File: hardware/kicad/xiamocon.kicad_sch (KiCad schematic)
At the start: 77 parts, among them J1 JST S2B-PH-SM4-TB, J2 Conn_01x02, J3 Micro_SD_Card_Det_Hirose_DM3AT, J4 Hong Cheng HC-PM254-5.0H-2x10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, Q1 IRLML6344TRPBF, Q2 IRLML6344TRPBF, Q3 IRLML2246TRPBF, Q4 IRLML2246TRPBF, Q5 IRLML2246TRPBF, SW1 GT-TC018A-H0375-L1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

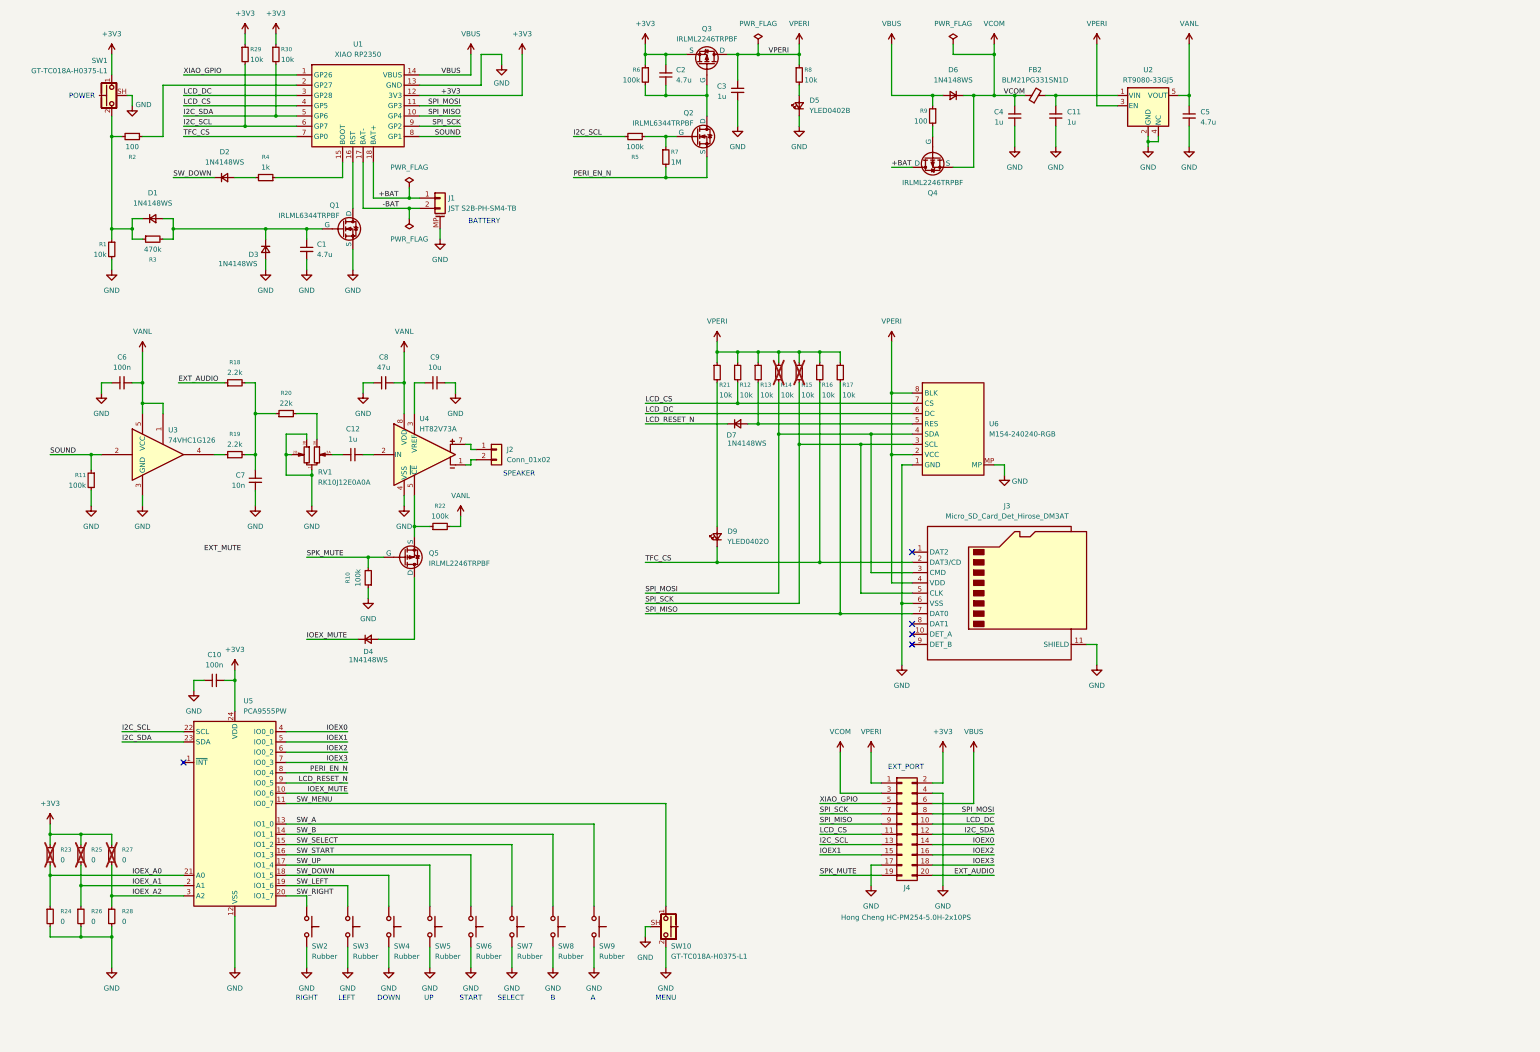
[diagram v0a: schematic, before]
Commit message: schematic fixed
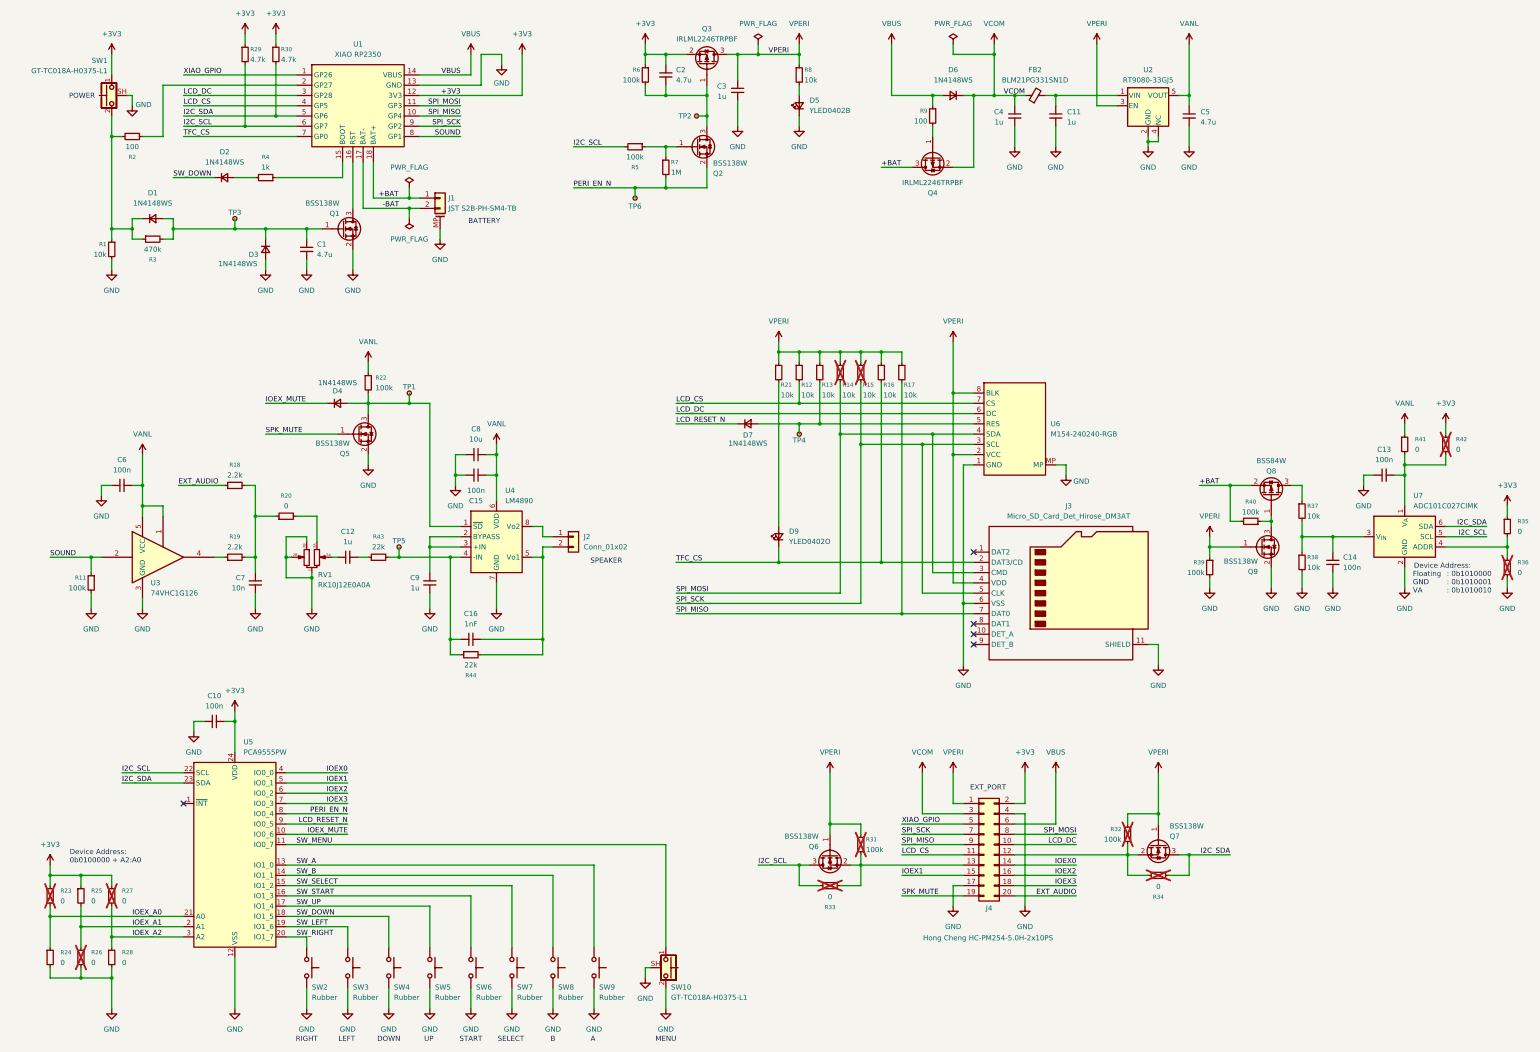
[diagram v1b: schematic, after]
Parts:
- removed Q1, Q2: IRLML6344TRPBF, Package_TO_SOT_SMD:SOT-23, symbol Simulation_SPICE:NMOS
- removed Q5: IRLML2246TRPBF, Package_TO_SOT_SMD:SOT-23, symbol Simulation_SPICE:PMOS
- removed R10: 100k, Resistor_SMD:R_0402_1005Metric, symbol Device:R_Small
- removed U4: HT82V73A, shpc_ic:SOIC-8_with_Thermal_Hole, symbol shpc_ic:HT82V73A
- added C13, C14, C15: 100n, Capacitor_SMD:C_0402_1005Metric, symbol Device:C_Small
- added C16: 1nF, Capacitor_SMD:C_0603_1608Metric, symbol Device:C_Small
- added Q1, Q2, Q5, Q6, Q7, Q9: BSS138W, Package_TO_SOT_SMD:SOT-323_SC-70, symbol Transistor_FET:Q_NMOS_GSD
- added Q8: BSS84W, Package_TO_SOT_SMD:SOT-323_SC-70, symbol Transistor_FET:Q_PMOS_GSD
- added R31, R32, R39, R40: 100k, Resistor_SMD:R_0402_1005Metric, symbol Device:R_Small
- added R33, R34, R35, R36, R41, R42: 0, Resistor_SMD:R_0402_1005Metric, symbol Device:R_Small
- added R37, R38: 10k, Resistor_SMD:R_0402_1005Metric, symbol Device:R_Small
- added R43, R44: 22k, Resistor_SMD:R_0402_1005Metric, symbol Device:R_Small
- added TP1, TP2, TP3, TP4, TP5, TP6: PWAMP_CE, TestPoint:TestPoint_Pad_D1.5mm, symbol Connector:TestPoint_Small
- added U4: LM4890, Package_SO:MSOP-8_3x3mm_P0.65mm, symbol shpc_ic:LM4890
- added U7: ADC101C027CIMK, Package_TO_SOT_SMD:SOT-23-6, symbol shpc_ic:ADC101C027CIMK
- C8: value 47u -> 10u; LCSC C140782 -> C1691; URL https://www.lcsc.com/product-detail/C140782.html -> https://www.lcsc.com/product-detail/C1691.html
- C9: value 10u -> 1u; LCSC C1691 -> C140782; URL https://www.lcsc.com/product-detail/C1691.html -> https://www.lcsc.com/product-detail/C140782.html
- D5, D9: footprint LED_SMD:LED_0402_1005Metric -> LED_SMD:LED_0402_1005Metric_Pad0.77x0.64mm_HandSolder
- Q3, Q4: symbol Simulation_SPICE:PMOS -> Transistor_FET:Q_PMOS_GSD
- R2, R9: LCSC C1545 -> C106232; URL https://www.lcsc.com/product-detail/C1545.html -> https://www.lcsc.com/product-detail/C106232.html
- R20: value 22k -> 0; LCSC C82868 -> C106231; URL https://www.lcsc.com/product-detail/C82868.html -> https://www.lcsc.com/product-detail/C106231.html
- R21, R8: footprint Resistor_SMD:R_0402_1005Metric -> Resistor_SMD:R_0402_1005Metric_Pad0.72x0.64mm_HandSolder
- R25: now fitted
- R26: now not fitted
- R29, R30: value 10k -> 4.7k; LCSC C60490 -> C105871; URL https://www.lcsc.com/product-detail/C60490.html -> https://www.lcsc.com/product-detail/C105871.html
- R5: LCSC C60490 -> C60491; URL https://www.lcsc.com/product-detail/C60490.html -> https://www.lcsc.com/product-detail/C60491.html
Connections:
- net +3V3: now also Q3.2 (S), R35.1, R42.1; no longer Q3.3 (S)
- net +BAT: now also Q4.3 (D), Q8.2 (S), R40.2; no longer Q4.1 (D)
- net GND: now also C8.2, C13.1, C14.1, C15.2, Q1.2 (S), Q5.2 (S), Q9.2 (S), R36.2, R38.2, R39.2, U4.7 (GND), U7.2 (GND); no longer C8.1
- net I2C_SCL: now also Q6.3 (D), R33.1, U7.5 (SCL); no longer J4.13 (Pin_13)
- net I2C_SDA: now also Q7.3 (D), R34.2, U7.6 (SDA); no longer J4.12 (Pin_12)
- net PERI_EN_N: now also Q2.2 (S), TP6.1
- net SPK_MUTE: now also Q5.1 (G)
- net VANL: now also C8.1, R22.1, C15.1, R41.1, U4.6 (VDD); no longer C8.2, R22.2
- net VCOM: now also Q4.2 (S); no longer Q4.3 (S)
- net VPERI: now also Q3.3 (D), Q6.1 (G), Q7.1 (G), Q9.1 (G), R31.1, R32.1, R39.1; no longer Q3.1 (D)
- net at J2.2 (Pin_2): now also C16.1, R44.2, U4.5 (Vo1)
- net at C12.2: now also R43.1
- net at C9.2: now also U4.2 (BYPASS), U4.3 (+IN)
- net at J2.1 (Pin_1): now also U4.8 (Vo2)
- net at R5.1, R7.1: now also Q2.1 (G)
- net at C2.2, R6.2: now also Q3.1 (G), Q2.3 (D), TP2.1; no longer Q3.2 (G)
- net at C1.1, D1.2 (A), D3.1 (K)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: now also Q1.1 (G), TP3.1
- net at D7.2 (A), R13.2, U6.5 (RES): now also TP4.1
- net at R9.2: now also Q4.1 (G); no longer Q4.2 (G)
- net at U1.16 (RST): now also Q1.3 (D)
- net at D4.2 (A): now also R22.2, Q5.3 (D), TP1.1, U4.1 (~{SD})
- new net: C16.2, R43.2, R44.1, TP5.1, U4.4 (-IN)
- new net: R35.2, R36.1, U7.4 (ADDR)
- new net: C13.2, R41.2, R42.2, U7.1 (V_{A})
- new net: J4.12 (Pin_12), Q7.2 (S), R32.2, R34.1
- new net: C14.2, R37.2, R38.1, U7.3 (V_{IN})
- new net: J4.13 (Pin_13), Q6.2 (S), R31.2, R33.2
- new net: Q8.1 (G), Q9.3 (D), R40.1
- new net: Q8.3 (D), R37.1
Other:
- note added: ": 0b1010000 : 0b1010001 : 0b1010010"
- note added: "Device Address:"
- note added: "Device Address: 0b0100000 + A2:A0"
- note added: "Floating GND VA"
- moved on the sheet: C10, C12, C6, C7, D4, D7, D9, J2, J3, J4, R11, R12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
